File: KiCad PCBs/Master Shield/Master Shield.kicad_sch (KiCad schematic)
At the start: 32 parts, among them J1 Power, J2 PWM, J3 Analog, J4 PWM, J5 Analog, J6 Communication

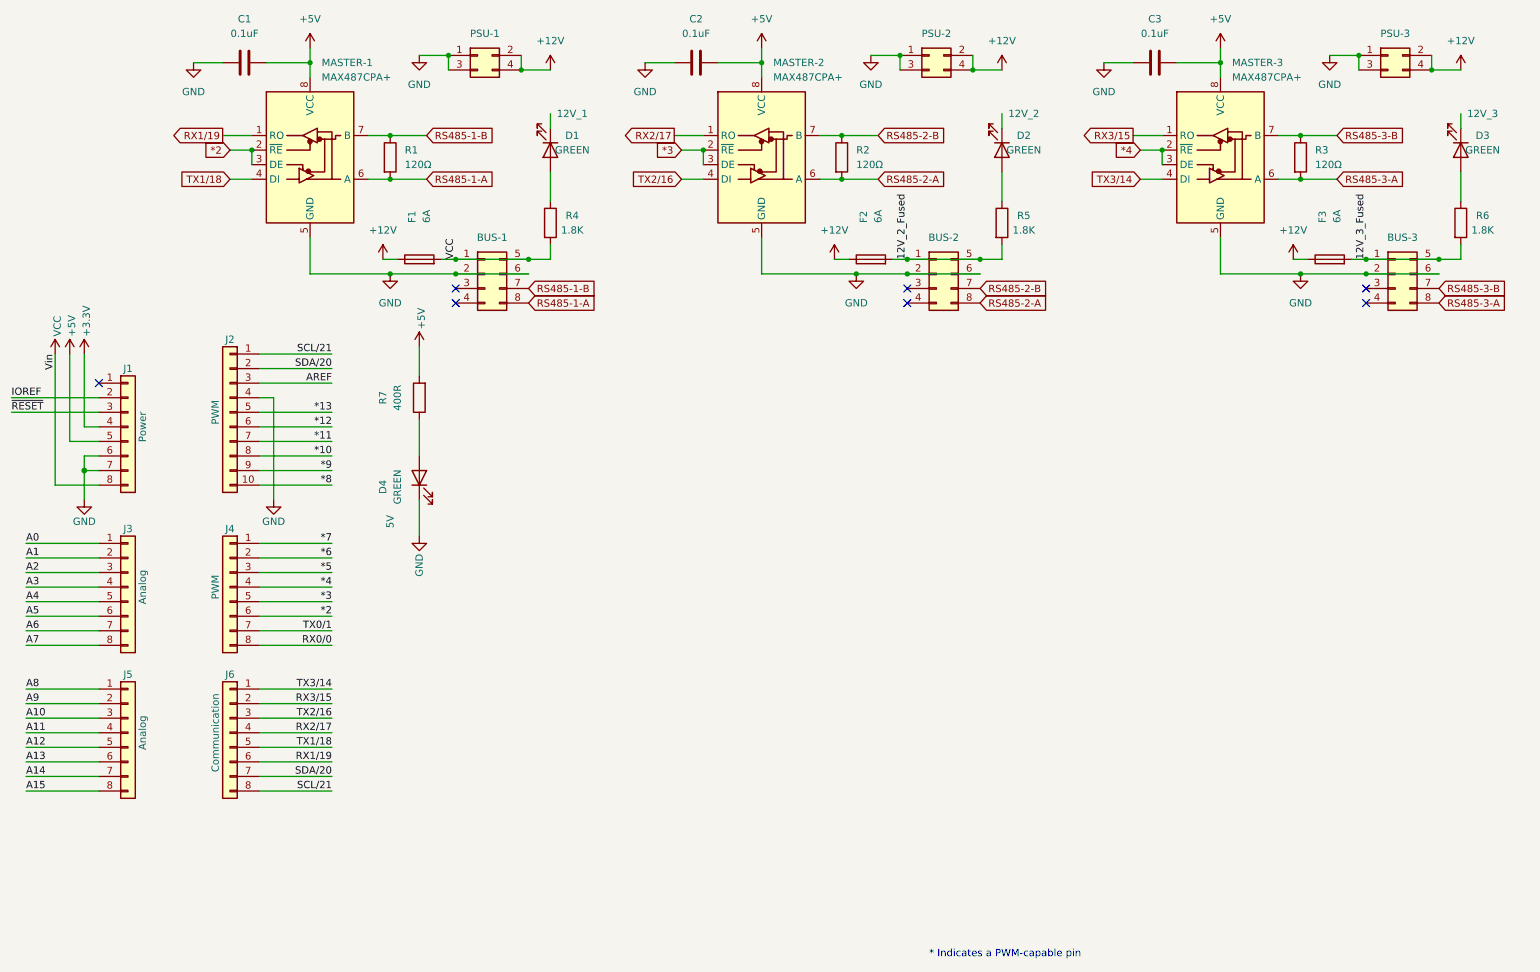
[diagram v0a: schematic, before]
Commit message: Completed first version of Master Shield
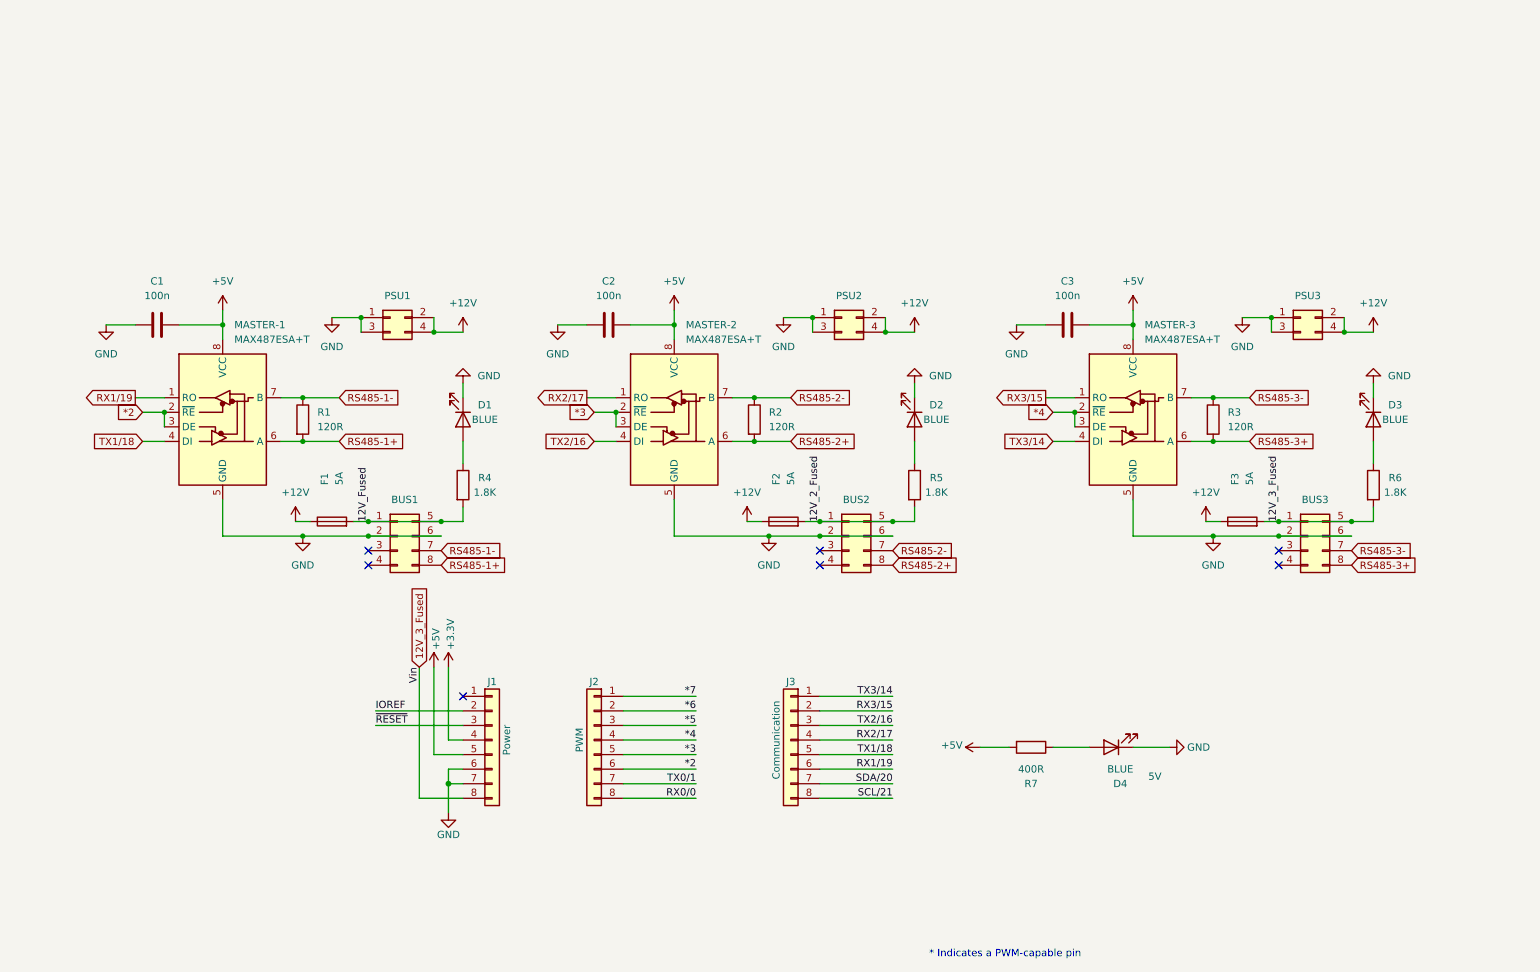
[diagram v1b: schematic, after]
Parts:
- removed J2: PWM, Connector_PinHeader_2.54mm:PinHeader_1x10_P2.54mm_Vertical, symbol Connector_Generic:Conn_01x10
- removed J3, J5: Analog, Connector_PinHeader_2.54mm:PinHeader_1x08_P2.54mm_Vertical, symbol Connector_Generic:Conn_01x08
- BUS1: renamed from BUS-1; footprint A10 KiCad Libraries:Molex 43045-0800 -> JLCPCB:CONN-TH_430450812
- BUS2: renamed from BUS-2; footprint A10 KiCad Libraries:Molex 43045-0800 -> JLCPCB:CONN-TH_430450812
- BUS3: renamed from BUS-3; footprint A10 KiCad Libraries:Molex 43045-0800 -> JLCPCB:CONN-TH_430450812
- C1, C2, C3: value 0.1uF -> 100n; footprint A10 KiCad Libraries:FA14 -> JLCPCB:C0402
- D1: value GREEN -> BLUE; footprint LED_SMD:LED_1210_3225Metric_Pad1.42x2.65mm_HandSolder -> LED_SMD:LED_0603_1608Metric; Field4 12V_1 -> (none)
- D2: value GREEN -> BLUE; footprint LED_SMD:LED_1210_3225Metric_Pad1.42x2.65mm_HandSolder -> LED_SMD:LED_0603_1608Metric; Field4 12V_2 -> (none)
- D3: value GREEN -> BLUE; footprint LED_SMD:LED_1210_3225Metric_Pad1.42x2.65mm_HandSolder -> LED_SMD:LED_0603_1608Metric; Field4 12V_3 -> (none)
- D4: value GREEN -> BLUE; footprint LED_SMD:LED_1210_3225Metric_Pad1.42x2.65mm_HandSolder -> LED_SMD:LED_0603_1608Metric
- F1, F2, F3: value 6A -> 5A
- MASTER-1, MASTER-2, MASTER-3: value MAX487CPA+ -> MAX487ESA+T; footprint Package_DIP:DIP-8_W7.62mm_LongPads -> JLCPCB:SOIC-8_L5.0-W4.0-P1.27-LS6.0-BL
- PSU1: renamed from PSU-1; footprint A10 KiCad Libraries:Molex 43045-0400 -> JLCPCB:CONN-TH_0430450400
- PSU2: renamed from PSU-2; footprint A10 KiCad Libraries:Molex 43045-0400 -> JLCPCB:CONN-TH_0430450400
- PSU3: renamed from PSU-3; footprint A10 KiCad Libraries:Molex 43045-0400 -> JLCPCB:CONN-TH_0430450400
- R1, R2, R3: value 120Ω -> 120R; footprint Resistor_THT:R_Axial_DIN0207_L6.3mm_D2.5mm_P7.62mm_Horizontal -> Resistor_SMD:R_0805_2012Metric
- R4, R5, R6, R7: footprint Resistor_SMD:R_1210_3225Metric_Pad1.30x2.65mm_HandSolder -> Resistor_SMD:R_0805_2012Metric
- renumbered J4 to J2, J6 to J3
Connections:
- net 12V_3_Fused: now also J1.8 (Pin_8)
- net GND: now also D1.1 (K), D2.1 (K), D3.1 (K)
- net RS485-1-A renamed RS485-1+
- net RS485-1-B renamed RS485-1-
- net RS485-2-A renamed RS485-2+
- net RS485-2-B renamed RS485-2-
- net RS485-3-A renamed RS485-3+
- net RS485-3-B renamed RS485-3-
- net VCC renamed 12V_Fused
- net 12V_Fused: no longer J1.8 (Pin_8)
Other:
- moved on the sheet: BUS1, BUS2, BUS3, C1, C2, C3, D1, D2, D3, D4, F1, F2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

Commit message: Final Master Shield files
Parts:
- BUS1, BUS2, BUS3: LCSC (none) -> C277661
- C1, C2, C3: LCSC (none) -> C1525
- D1, D2, D3: LCSC (none) -> C72041
- D4: Field4 5V -> (none); LCSC (none) -> C72041
- F1, F2, F3, PSU1, PSU2, PSU3: now left out of the parts list
- J1, J2, J3: LCSC (none) -> C124381
- MASTER-1, MASTER-2, MASTER-3: LCSC (none) -> C9953
- R1, R2, R3: LCSC (none) -> C17437
- R4, R5, R6: LCSC (none) -> C17398
- R7: LCSC (none) -> C17655
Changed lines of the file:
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@@
     )
     (property "Datasheet" "" (id 3) (at 101.6 142.24 0))
+    (property "LCSC" "C124381" (id 4) (at 101.6 142.24 0)
+      (effects (font (size 1.27 1.27)) hide)
+    )
     (pin "1")
     (pin "2")
@@
     )
     (property "Datasheet" "" (id 3) (at 119.38 142.24 0))
+    (property "LCSC" "C124381" (id 4) (at 119.38 142.24 0)
+      (effects (font (size 1.27 1.27)) hide)
+    )
     (pin "1")
     (pin "2")
@@
     )
     (property "Datasheet" "" (id 3) (at 153.67 142.24 0))
+    (property "LCSC" "C124381" (id 4) (at 153.67 142.24 0)
+      (effects (font (size 1.27 1.27)) hide)
+    )
     (pin "1")
     (pin "2")
@@
       (effects (font (size 1.27 1.27)) hide)
     )
+    (property "LCSC" "C9953" (id 4) (at 133.35 85.09 0)
+      (effects (font (size 1.27 1.27)) hide)
+    )
     (pin "1")
     (pin "2")
@@
       (effects (font (size 1.27 1.27)) hide)
     )
+    (property "LCSC" "C72041" (id 4) (at 175.26 86.36 0)
+      (effects (font (size 1.27 1.27)) hide)
+    )
     (pin "1")
     (pin "2")
   )
   (symbol (lib_id "Device:Fuse") (at 73.66 104.14 90) (unit 1)
-    (in_bom yes) (on_board yes)
+    (in_bom no) (on_board yes)
     (property "Reference" "F1" (id 0) (at 72.3899 97.79 0)
       (effects (font (size 1.27 1.27)) (justify left))
@@
   )
   (symbol (lib_id "Connector_Generic:Conn_02x02_Odd_Even") (at 83.82 68.58 0) (unit 1)
-    (in_bom yes) (on_board yes)
+    (in_bom no) (on_board yes)
     (property "Reference" "PSU1" (id 0) (at 85.09 64.77 0))
     (property "Value" "Conn_02x02_Top_Bottom" (id 1) (at 85.09 64.77 0)
@@
       (effects (font (size 1.27 1.27)) hide)
     )
+    (property "LCSC" "C17655" (id 4) (at 195.58 143.51 0)
+      (effects (font (size 1.27 1.27)) hide)
+    )
     (pin "1")
     (pin "2")
@@
     )
     (property "Datasheet" "https://datasheets.maximintegrated.com/en/ds/MAX1487E-MAX491E.pdf" (id 3) (at 213.36 83.82 0)
+      (effects (font (size 1.27 1.27)) hide)
+    )
+    (property "LCSC" "C9953" (id 4) (at 213.36 85.09 0)
       (effects (font (size 1.27 1.27)) hide)
     )
@@
       (effects (font (size 1.27 1.27)) hide)
     )
+    (property "LCSC" "C277661" (id 4) (at 243.84 106.68 0)
+      (effects (font (size 1.27 1.27)) hide)
+    )
     (pin "1")
     (pin "2")
@@
       (effects (font (size 1.27 1.27)) hide)
     )
+    (property "LCSC" "C1525" (id 4) (at 201.93 69.85 0)
+      (effects (font (size 1.27 1.27)) hide)
+    )
     (pin "1")
     (pin "2")
@@
     )
     (property "Datasheet" "~" (id 3) (at 85.09 106.68 0)
+      (effects (font (size 1.27 1.27)) hide)
+    )
+    (property "LCSC" "C277661" (id 4) (at 85.09 106.68 0)
       (effects (font (size 1.27 1.27)) hide)
     )
@@
       (effects (font (size 1.27 1.27)) hide)
     )
+    (property "LCSC" "C17437" (id 4) (at 147.32 86.36 0)
+      (effects (font (size 1.27 1.27)) hide)
+    )
     (pin "1")
     (pin "2")
@@
   )
   (symbol (lib_id "Device:Fuse") (at 152.4 104.14 90) (unit 1)
-    (in_bom yes) (on_board yes)
+    (in_bom no) (on_board yes)
     (property "Reference" "F2" (id 0) (at 151.1299 97.79 0)
       (effects (font (size 1.27 1.27)) (justify left))
@@
   )
   (symbol (lib_id "Connector_Generic:Conn_02x02_Odd_Even") (at 162.56 68.58 0) (unit 1)
-    (in_bom yes) (on_board yes) (fields_autoplaced)
+    (in_bom no) (on_board yes) (fields_autoplaced)
     (property "Reference" "PSU2" (id 0) (at 163.83 64.77 0))
     (property "Value" "Conn_02x02_Top_Bottom" (id 1) (at 163.83 64.77 0)
@@
       (effects (font (size 1.27 1.27)) hide)
     )
-    (property "Field4" "5V" (id 4) (at 217.17 148.59 0))
+    (property "LCSC" "C72041" (id 4) (at 209.55 143.51 0)
+      (effects (font (size 1.27 1.27)) hide)
+    )
     (pin "1")
     (pin "2")
@@
       (effects (font (size 1.27 1.27)) hide)
     )
+    (property "LCSC" "C17398" (id 4) (at 96.52 97.79 0)
+      (effects (font (size 1.27 1.27)) hide)
+    )
     (pin "1")
     (pin "2")
@@
     )
     (property "Datasheet" "~" (id 3) (at 163.83 106.68 0)
+      (effects (font (size 1.27 1.27)) hide)
+    )
+    (property "LCSC" "C277661" (id 4) (at 163.83 106.68 0)
       (effects (font (size 1.27 1.27)) hide)
     )
@@
       (effects (font (size 1.27 1.27)) hide)
     )
+    (property "LCSC" "C17437" (id 4) (at 68.58 86.36 0)
+      (effects (font (size 1.27 1.27)) hide)
+    )
     (pin "1")
     (pin "2")
@@
   )
   (symbol (lib_id "Device:Fuse") (at 232.41 104.14 90) (unit 1)
-    (in_bom yes) (on_board yes)
+    (in_bom no) (on_board yes)
     (property "Reference" "F3" (id 0) (at 231.1399 97.79 0)
       (effects (font (size 1.27 1.27)) (justify left))
@@
       (effects (font (size 1.27 1.27)) hide)
     )
+    (property "LCSC" "C1525" (id 4) (at 121.92 69.85 0)
+      (effects (font (size 1.27 1.27)) hide)
+    )
     (pin "1")
     (pin "2")
@@
       (effects (font (size 1.27 1.27)) hide)
     )
+    (property "LCSC" "C1525" (id 4) (at 43.18 69.85 0)
+      (effects (font (size 1.27 1.27)) hide)
+    )
     (pin "1")
     (pin "2")
   )
   (symbol (lib_id "Connector_Generic:Conn_02x02_Odd_Even") (at 242.57 68.58 0) (unit 1)
-    (in_bom yes) (on_board yes) (fields_autoplaced)
+    (in_bom no) (on_board yes) (fields_autoplaced)
     (property "Reference" "PSU3" (id 0) (at 243.84 64.77 0))
     (property "Value" "Conn_02x02_Top_Bottom" (id 1) (at 243.84 64.77 0)
@@
     )
     (property "Datasheet" "https://datasheets.maximintegrated.com/en/ds/MAX1487E-MAX491E.pdf" (id 3) (at 54.61 83.82 0)
+      (effects (font (size 1.27 1.27)) hide)
+    )
+    (property "LCSC" "C9953" (id 4) (at 54.61 85.09 0)
       (effects (font (size 1.27 1.27)) hide)
     )
@@
       (effects (font (size 1.27 1.27)) hide)
     )
+    (property "LCSC" "C17437" (id 4) (at 227.33 86.36 0)
+      (effects (font (size 1.27 1.27)) hide)
+    )
     (pin "1")
     (pin "2")
@@
       (effects (font (size 1.27 1.27)) hide)
     )
+    (property "LCSC" "C17398" (id 4) (at 255.27 97.79 0)
+      (effects (font (size 1.27 1.27)) hide)
+    )
     (pin "1")
     (pin "2")
@@
       (effects (font (size 1.27 1.27)) hide)
     )
+    (property "LCSC" "C72041" (id 4) (at 255.27 86.36 0)
+      (effects (font (size 1.27 1.27)) hide)
+    )
     (pin "1")
     (pin "2")
@@
       (effects (font (size 1.27 1.27)) hide)
     )
+    (property "LCSC" "C72041" (id 4) (at 96.52 86.36 0)
+      (effects (font (size 1.27 1.27)) hide)
+    )
     (pin "1")
     (pin "2")
@@
       (effects (font (size 1.27 1.27)) hide)
     )
+    (property "LCSC" "C17398" (id 4) (at 175.26 97.79 0)
+      (effects (font (size 1.27 1.27)) hide)
+    )

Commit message: Updated LCSC number for fuse
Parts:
- F1, F2, F3: LCSC (none) -> C492610
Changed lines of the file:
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@@
+      (effects (font (size 1.27 1.27)) hide)
+    )
+    (property "LCSC" "C492610" (id 4) (at 73.66 104.14 0)
       (effects (font (size 1.27 1.27)) hide)
     )
@@
       (effects (font (size 1.27 1.27)) hide)
     )
+    (property "LCSC" "C492610" (id 4) (at 152.4 104.14 0)
+      (effects (font (size 1.27 1.27)) hide)
+    )
     (pin "1")
     (pin "2")
@@
       (effects (font (size 1.27 1.27)) hide)
     )
+    (property "LCSC" "C492610" (id 4) (at 232.41 104.14 0)
+      (effects (font (size 1.27 1.27)) hide)
+    )
